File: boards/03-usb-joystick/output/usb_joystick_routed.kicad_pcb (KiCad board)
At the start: 2 copper layers, 80 x 60 mm, 12 parts, among them J1 USB-C, SW1 Button, SW2 Button, SW3 Button, SW4 Button, U1 MCU, Y1 16MHz

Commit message: style(router): Use set comprehension instead of generator
Co-Authored-By: Claude Opus 4.5 <noreply@anthropic.com>
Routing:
- net BTN1: track 38.2 -> 0.00 mm
- net BTN4: track 35.4 -> 0.00 mm
- net XTAL2: track 26.7 -> 0.00 mm, vias 2 -> 0
- net JOY_Y: track 25.1 -> 0.00 mm
- net USB_CC1: track 24.7 -> 0.00 mm, vias 2 -> 0
- net BTN2: track 24.0 -> 0.00 mm, vias 2 -> 0
- net JOY_X: track 23.7 -> 0.00 mm
- net JOY_BTN: track 21.7 -> 0.00 mm, vias 2 -> 0
- net BTN3: track 21.4 -> 0.00 mm
- net XTAL1: track 20.5 -> 0.00 mm
- net USB_CC2: track 19.5 -> 0.00 mm

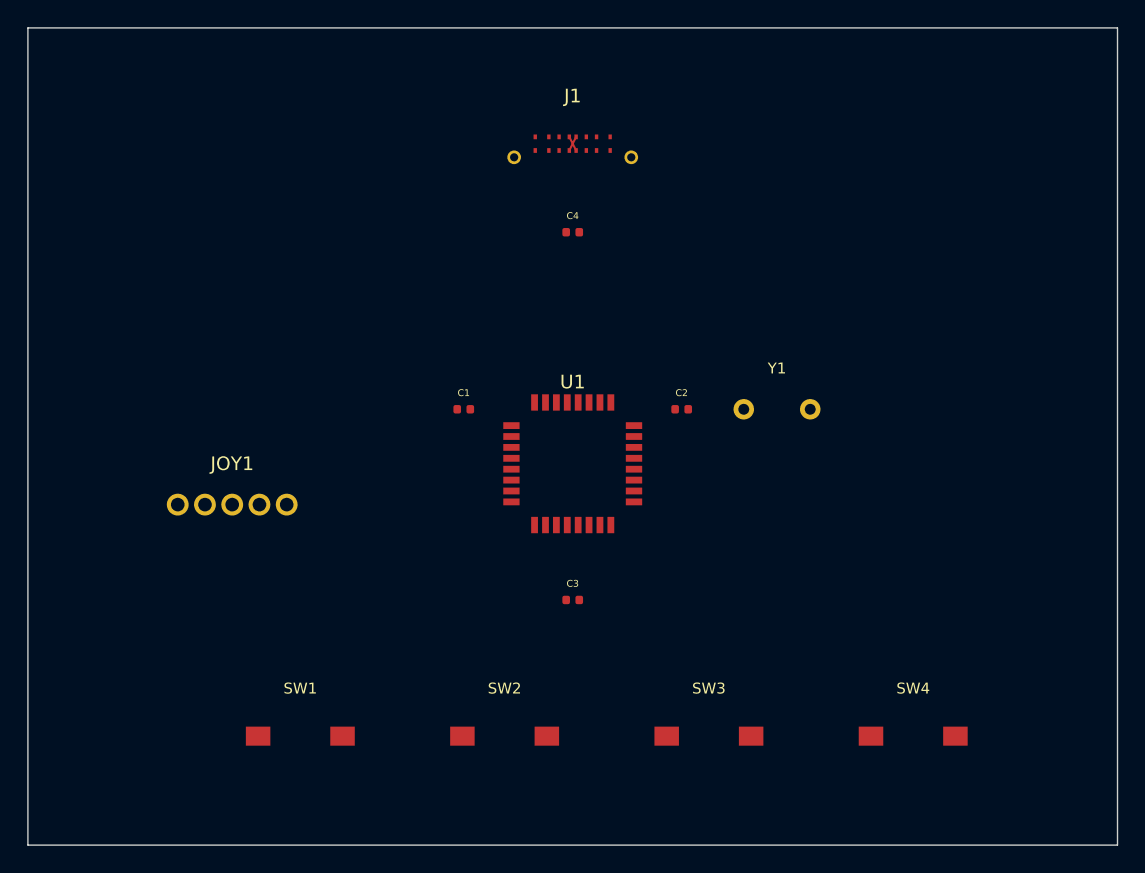
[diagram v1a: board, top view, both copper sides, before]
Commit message: fix(board): Increase silkscreen text height for board 03 components (#867)
Update footprint generation to use 1.0mm text height (JLCPCB minimum):
- Crystal (Y1): 0.80mm → 1.0mm
- Buttons (SW1-SW4): 0.80mm → 1.0mm
- Capacitors (C1-C4): 0.50mm → 1.0mm

This matches the fixes applied to boards 00 and 02 (issues #859, #865).

Co-Authored-By: Claude Opus 4.5 <noreply@anthropic.com>
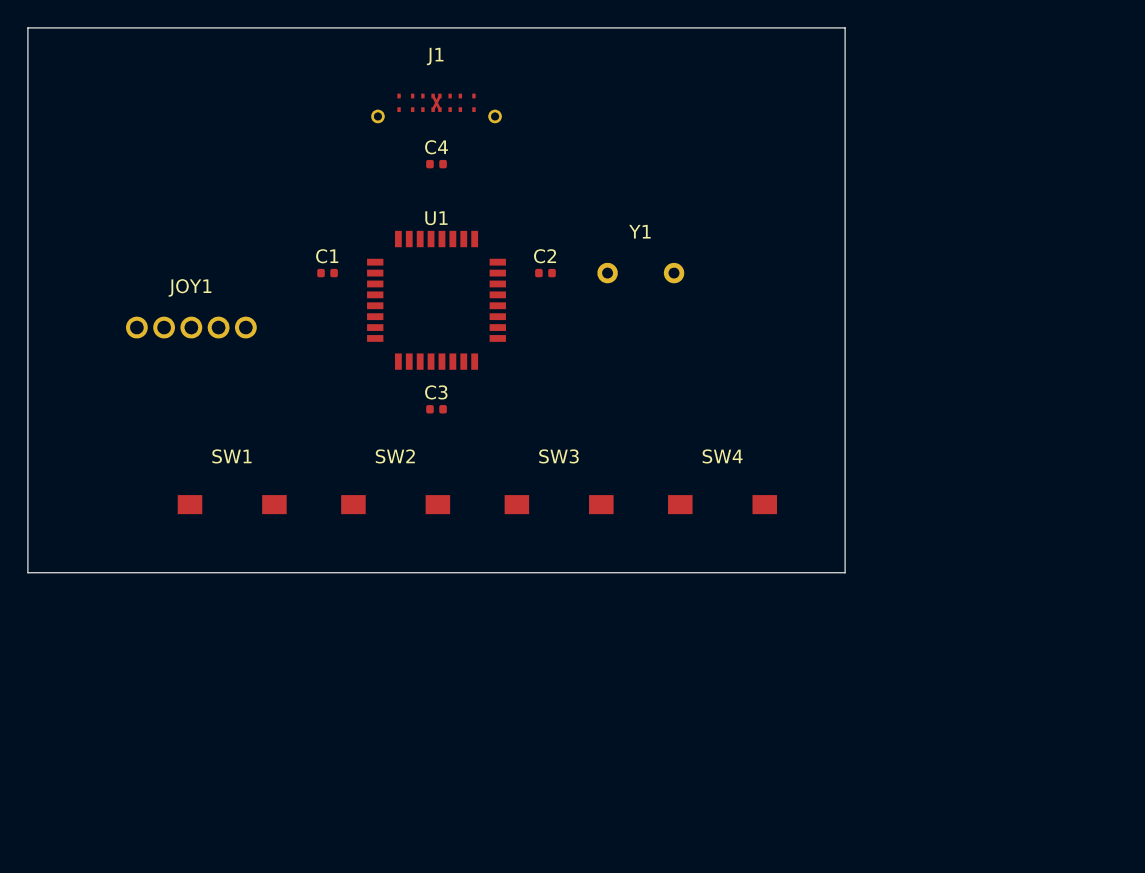
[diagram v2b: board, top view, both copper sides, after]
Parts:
- moved SW4 22.0 mm to (151.0, 135.0)
- moved SW3 20.2 mm to (139.0, 135.0)
- moved SW2 18.8 mm to (127.0, 135.0)
- moved SW1 17.7 mm to (115.0, 135.0)
- moved C3 17.2 mm to (130.0, 128.0)
- moved U1 15.6 mm to (130.0, 120.0)
- moved C1 14.1 mm to (122.0, 118.0)
- moved C2 14.1 mm to (138.0, 118.0)
- moved Y1 14.1 mm to (145.0, 118.0)
- moved JOY1 13.3 mm to (112.0, 122.0)
- moved C4 11.2 mm to (130.0, 110.0)
- moved J1 10.4 mm to (130.0, 105.0)
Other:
- board size 80 x 60 mm -> 60 x 40 mm
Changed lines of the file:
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@@
   (net 15 "XTAL1")
   (net 16 "XTAL2")
-  (gr_rect (start 100.0 100.0) (end 180.0 160.0)
+  (gr_rect (start 100.0 100.0) (end 160.0 140.0)
     (stroke (width 0.1) (type default))
     (fill none)
@@
   (footprint "Package_QFP:TQFP-32_7x7mm_P0.8mm"
     (layer "F.Cu")
-    (at 140.0 132.0)
+    (at 130.0 120.0)
     (fp_text reference "U1" (at 0 -6) (layer "F.SilkS")
       (effects (font (size 1 1) (thickness 0.15)))
@@
   (footprint "Connector_USB:USB_C_Receptacle_GCT_USB4105"
     (layer "F.Cu")
-    (at 140.0 108.0)
+    (at 130.0 105.0)
     (fp_text reference "J1" (at 0 -3) (layer "F.SilkS")
       (effects (font (size 1 1) (thickness 0.15)))
@@
   (footprint "Module:Joystick_Analog"
     (layer "F.Cu")
-    (at 115.0 135.0)
+    (at 112.0 122.0)
     (fp_text reference "JOY1" (at 0 -3) (layer "F.SilkS")
       (effects (font (size 1 1) (thickness 0.15)))
@@
   (footprint "Crystal:Crystal_HC49-U_Vertical"
     (layer "F.Cu")
-    (at 155.0 128.0)
+    (at 145.0 118.0)
     (fp_text reference "Y1" (at 0 -3) (layer "F.SilkS")
-      (effects (font (size 0.8 0.8) (thickness 0.12)))
+      (effects (font (size 1 1) (thickness 0.15)))
     )
     (fp_text value "16MHz" (at 0 3) (layer "F.Fab")
-      (effects (font (size 0.8 0.8) (thickness 0.12)))
+      (effects (font (size 1 1) (thickness 0.15)))
     )
     (pad "1" thru_hole circle (at -2.44 0) (size 1.5 1.5) (drill 0.8) (layers "*.Cu" "*.Mask") (net 15 "XTAL1"))
@@
   (footprint "Button_Switch_SMD:SW_SPST_TL3342"
     (layer "F.Cu")
-    (at 120.0 152.0)
+    (at 115.0 135.0)
     (fp_text reference "SW1" (at 0 -3.5) (layer "F.SilkS")
-      (effects (font (size 0.8 0.8) (thickness 0.12)))
-    )
-    (fp_text value "Button" (at 0 3.5) (layer "F.Fab")
-      (effects (font (size 0.8 0.8) (thickness 0.12)))
+      (effects (font (size 1 1) (thickness 0.15)))
+    )
+    (fp_text value "Button" (at 0 3.5) (layer "F.Fab")
+      (effects (font (size 1 1) (thickness 0.15)))
     )
     (pad "1" smd rect (at -3.1 0) (size 1.8 1.4) (layers "F.Cu" "F.Paste" "F.Mask") (net 11 "BTN1"))
@@
   (footprint "Button_Switch_SMD:SW_SPST_TL3342"
     (layer "F.Cu")
-    (at 135.0 152.0)
+    (at 127.0 135.0)
     (fp_text reference "SW2" (at 0 -3.5) (layer "F.SilkS")
-      (effects (font (size 0.8 0.8) (thickness 0.12)))
-    )
-    (fp_text value "Button" (at 0 3.5) (layer "F.Fab")
-      (effects (font (size 0.8 0.8) (thickness 0.12)))
+      (effects (font (size 1 1) (thickness 0.15)))
+    )
+    (fp_text value "Button" (at 0 3.5) (layer "F.Fab")
+      (effects (font (size 1 1) (thickness 0.15)))
     )
     (pad "1" smd rect (at -3.1 0) (size 1.8 1.4) (layers "F.Cu" "F.Paste" "F.Mask") (net 12 "BTN2"))
@@
   (footprint "Button_Switch_SMD:SW_SPST_TL3342"
     (layer "F.Cu")
-    (at 150.0 152.0)
+    (at 139.0 135.0)
     (fp_text reference "SW3" (at 0 -3.5) (layer "F.SilkS")
-      (effects (font (size 0.8 0.8) (thickness 0.12)))
-    )
-    (fp_text value "Button" (at 0 3.5) (layer "F.Fab")
-      (effects (font (size 0.8 0.8) (thickness 0.12)))
+      (effects (font (size 1 1) (thickness 0.15)))
+    )
+    (fp_text value "Button" (at 0 3.5) (layer "F.Fab")
+      (effects (font (size 1 1) (thickness 0.15)))
     )
     (pad "1" smd rect (at -3.1 0) (size 1.8 1.4) (layers "F.Cu" "F.Paste" "F.Mask") (net 13 "BTN3"))
@@
   (footprint "Button_Switch_SMD:SW_SPST_TL3342"
     (layer "F.Cu")
-    (at 165.0 152.0)
+    (at 151.0 135.0)
     (fp_text reference "SW4" (at 0 -3.5) (layer "F.SilkS")
-      (effects (font (size 0.8 0.8) (thickness 0.12)))
-    )
-    (fp_text value "Button" (at 0 3.5) (layer "F.Fab")
-      (effects (font (size 0.8 0.8) (thickness 0.12)))
+      (effects (font (size 1 1) (thickness 0.15)))
+    )
+    (fp_text value "Button" (at 0 3.5) (layer "F.Fab")
+      (effects (font (size 1 1) (thickness 0.15)))
     )
     (pad "1" smd rect (at -3.1 0) (size 1.8 1.4) (layers "F.Cu" "F.Paste" "F.Mask") (net 14 "BTN4"))
@@
   (footprint "Capacitor_SMD:C_0402_1005Metric"
     (layer "F.Cu")
-    (at 132.0 128.0)
+    (at 122.0 118.0)
     (fp_text reference "C1" (at 0 -1.2) (layer "F.SilkS")
-      (effects (font (size 0.5 0.5) (thickness 0.1)))
-    )
-    (fp_text value "100nF" (at 0 1.2) (layer "F.Fab")
-      (effects (font (size 0.5 0.5) (thickness 0.1)))
+      (effects (font (size 1 1) (thickness 0.15)))
+    )
+    (fp_text value "100nF" (at 0 1.2) (layer "F.Fab")
+      (effects (font (size 1 1) (thickness 0.15)))
     )
     (pad "1" smd roundrect (at -0.48 0) (size 0.56 0.62) (layers "F.Cu" "F.Paste" "F.Mask") (roundrect_rratio 0.25) (net 2 "VCC"))
@@
   (footprint "Capacitor_SMD:C_0402_1005Metric"
     (layer "F.Cu")
-    (at 148.0 128.0)
+    (at 138.0 118.0)
     (fp_text reference "C2" (at 0 -1.2) (layer "F.SilkS")
-      (effects (font (size 0.5 0.5) (thickness 0.1)))
-    )
-    (fp_text value "100nF" (at 0 1.2) (layer "F.Fab")
-      (effects (font (size 0.5 0.5) (thickness 0.1)))
+      (effects (font (size 1 1) (thickness 0.15)))
+    )
+    (fp_text value "100nF" (at 0 1.2) (layer "F.Fab")
+      (effects (font (size 1 1) (thickness 0.15)))
     )
     (pad "1" smd roundrect (at -0.48 0) (size 0.56 0.62) (layers "F.Cu" "F.Paste" "F.Mask") (roundrect_rratio 0.25) (net 2 "VCC"))
@@
   (footprint "Capacitor_SMD:C_0402_1005Metric"
     (layer "F.Cu")
-    (at 140.0 142.0)
+    (at 130.0 128.0)
     (fp_text reference "C3" (at 0 -1.2) (layer "F.SilkS")
-      (effects (font (size 0.5 0.5) (thickness 0.1)))
-    )
-    (fp_text value "100nF" (at 0 1.2) (layer "F.Fab")
-      (effects (font (size 0.5 0.5) (thickness 0.1)))
+      (effects (font (size 1 1) (thickness 0.15)))
+    )
+    (fp_text value "100nF" (at 0 1.2) (layer "F.Fab")
+      (effects (font (size 1 1) (thickness 0.15)))
     )
     (pad "1" smd roundrect (at -0.48 0) (size 0.56 0.62) (layers "F.Cu" "F.Paste" "F.Mask") (roundrect_rratio 0.25) (net 2 "VCC"))
@@
   (footprint "Capacitor_SMD:C_0402_1005Metric"
     (layer "F.Cu")
-    (at 140.0 115.0)
+    (at 130.0 110.0)
     (fp_text reference "C4" (at 0 -1.2) (layer "F.SilkS")
-      (effects (font (size 0.5 0.5) (thickness 0.1)))
-    )
-    (fp_text value "100nF" (at 0 1.2) (layer "F.Fab")
-      (effects (font (size 0.5 0.5) (thickness 0.1)))
+      (effects (font (size 1 1) (thickness 0.15)))
+    )
+    (fp_text value "100nF" (at 0 1.2) (layer "F.Fab")
+      (effects (font (size 1 1) (thickness 0.15)))
     )
     (pad "1" smd roundrect (at -0.48 0) (size 0.56 0.62) (layers "F.Cu" "F.Paste" "F.Mask") (roundrect_rratio 0.25) (net 1 "VBUS"))
@@
   )
   (segment
-		(start 139.7500 109.0000)
-		(end 140.2500 108.0000)
-		(width 0.15)
+		(start 129.7500 106.0000)
+		(end 130.2500 105.0000)
+		(width 0.2)
 		(layer "F.Cu")
 		(net 5)
 	)
 	(segment
-		(start 139.7500 108.0000)
-		(end 140.2500 109.0000)
-		(width 0.15)
+		(start 129.7500 105.0000)
+		(end 130.2500 106.0000)
+		(width 0.2)
 		(layer "F.Cu")
 		(net 4)

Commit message: fix(boards): rename JOY1 to J2 in USB joystick board generators and outputs (#1530)
The joystick footprint generators used a non-standard reference designator
(JOY1) that mismatched the schematic and project spec (J2), causing
bom_pcb_match and bom_cpl_match preflight failures during kct export.

Co-authored-by: Claude Opus 4.6 <noreply@anthropic.com>
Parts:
- renumbered JOY1 to J2
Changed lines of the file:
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@@
     (layer "F.Cu")
     (at 112.0 122.0)
-    (fp_text reference "JOY1" (at 0 -3) (layer "F.SilkS")
+    (fp_text reference "J2" (at 0 -3) (layer "F.SilkS")
       (effects (font (size 1 1) (thickness 0.15)))
     )

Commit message: fix(boards): connect unused MCU pins to GND in boards 02 and 03
Unused MCU digital input pins were left without net assignments in the
PCB generators, producing pads with no net clause in the KiCad PCB
files. JLCPCB's automated review flags these unconnected pads and holds
orders for clarification. Connect all unused inputs to GND -- standard
practice that prevents floating inputs and eliminates review holds.

Board 02: pins 5, 6 (GND net 10)
Board 03: pins 5, 6, 18, 19, 20, 21, 22, 31 (GND net 3)

Co-Authored-By: Claude Opus 4.6 <noreply@anthropic.com>
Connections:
- U1 pad 18: (no net) -> GND
- U1 pad 19: (no net) -> GND
- U1 pad 20: (no net) -> GND
- U1 pad 21: (no net) -> GND
- U1 pad 22: (no net) -> GND
- U1 pad 31: (no net) -> GND
- U1 pad 5: (no net) -> GND
- U1 pad 6: (no net) -> GND
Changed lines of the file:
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@@
     (pad "3" smd rect (at -4.500 -1.200) (size 1.2 0.5) (layers "F.Cu" "F.Paste" "F.Mask") (net 16 "XTAL2"))
     (pad "4" smd rect (at -4.500 -0.400) (size 1.2 0.5) (layers "F.Cu" "F.Paste" "F.Mask") (net 2 "VCC"))
-    (pad "5" smd rect (at -4.500 0.400) (size 1.2 0.5) (layers "F.Cu" "F.Paste" "F.Mask") )
-    (pad "6" smd rect (at -4.500 1.200) (size 1.2 0.5) (layers "F.Cu" "F.Paste" "F.Mask") )
+    (pad "5" smd rect (at -4.500 0.400) (size 1.2 0.5) (layers "F.Cu" "F.Paste" "F.Mask") (net 3 "GND"))
+    (pad "6" smd rect (at -4.500 1.200) (size 1.2 0.5) (layers "F.Cu" "F.Paste" "F.Mask") (net 3 "GND"))
     (pad "7" smd rect (at -4.500 2.000) (size 1.2 0.5) (layers "F.Cu" "F.Paste" "F.Mask") (net 3 "GND"))
     (pad "8" smd rect (at -4.500 2.800) (size 1.2 0.5) (layers "F.Cu" "F.Paste" "F.Mask") (net 2 "VCC"))
@@
     (pad "16" smd rect (at 2.800 4.500) (size 0.5 1.2) (layers "F.Cu" "F.Paste" "F.Mask") (net 3 "GND"))
     (pad "17" smd rect (at 4.500 -2.800) (size 1.2 0.5) (layers "F.Cu" "F.Paste" "F.Mask") (net 2 "VCC"))
-    (pad "18" smd rect (at 4.500 -2.000) (size 1.2 0.5) (layers "F.Cu" "F.Paste" "F.Mask") )
-    (pad "19" smd rect (at 4.500 -1.200) (size 1.2 0.5) (layers "F.Cu" "F.Paste" "F.Mask") )
-    (pad "20" smd rect (at 4.500 -0.400) (size 1.2 0.5) (layers "F.Cu" "F.Paste" "F.Mask") )
-    (pad "21" smd rect (at 4.500 0.400) (size 1.2 0.5) (layers "F.Cu" "F.Paste" "F.Mask") )
-    (pad "22" smd rect (at 4.500 1.200) (size 1.2 0.5) (layers "F.Cu" "F.Paste" "F.Mask") )
+    (pad "18" smd rect (at 4.500 -2.000) (size 1.2 0.5) (layers "F.Cu" "F.Paste" "F.Mask") (net 3 "GND"))
+    (pad "19" smd rect (at 4.500 -1.200) (size 1.2 0.5) (layers "F.Cu" "F.Paste" "F.Mask") (net 3 "GND"))
+    (pad "20" smd rect (at 4.500 -0.400) (size 1.2 0.5) (layers "F.Cu" "F.Paste" "F.Mask") (net 3 "GND"))
+    (pad "21" smd rect (at 4.500 0.400) (size 1.2 0.5) (layers "F.Cu" "F.Paste" "F.Mask") (net 3 "GND"))
+    (pad "22" smd rect (at 4.500 1.200) (size 1.2 0.5) (layers "F.Cu" "F.Paste" "F.Mask") (net 3 "GND"))
     (pad "23" smd rect (at 4.500 2.000) (size 1.2 0.5) (layers "F.Cu" "F.Paste" "F.Mask") (net 3 "GND"))
     (pad "24" smd rect (at 4.500 2.800) (size 1.2 0.5) (layers "F.Cu" "F.Paste" "F.Mask") (net 2 "VCC"))
@@
     (pad "29" smd rect (at -0.400 -4.500) (size 0.5 1.2) (layers "F.Cu" "F.Paste" "F.Mask") (net 4 "USB_D+"))
     (pad "30" smd rect (at -1.200 -4.500) (size 0.5 1.2) (layers "F.Cu" "F.Paste" "F.Mask") (net 1 "VBUS"))
-    (pad "31" smd rect (at -2.000 -4.500) (size 0.5 1.2) (layers "F.Cu" "F.Paste" "F.Mask") )
+    (pad "31" smd rect (at -2.000 -4.500) (size 0.5 1.2) (layers "F.Cu" "F.Paste" "F.Mask") (net 3 "GND"))
     (pad "32" smd rect (at -2.800 -4.500) (size 0.5 1.2) (layers "F.Cu" "F.Paste" "F.Mask") (net 3 "GND"))
   )
